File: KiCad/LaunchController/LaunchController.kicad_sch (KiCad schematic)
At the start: 37 parts, among them J1 CONN_ICSP, J13 CONN_7SEG, J2 CONN_USB, J3 USB_B_Micro, U1 FT232RL, U2 ATMEGA2560-16AUR, Y1 HUSG-16.000-20

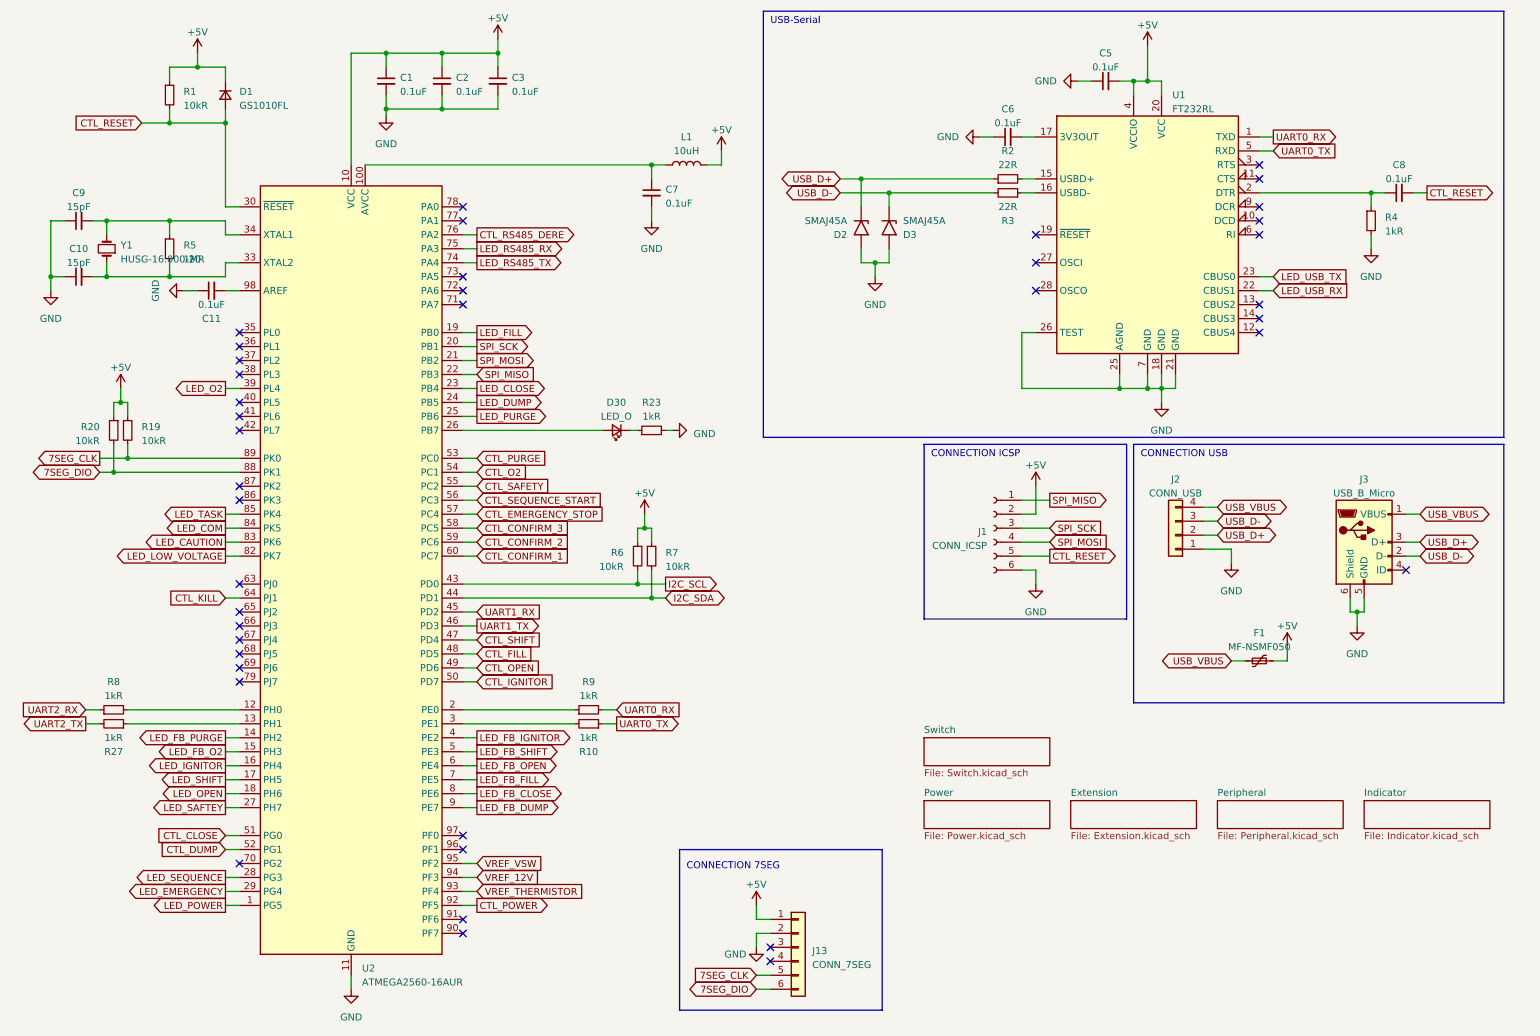
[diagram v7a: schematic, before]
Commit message: USBのTX，RXを統合してACCESSに変更
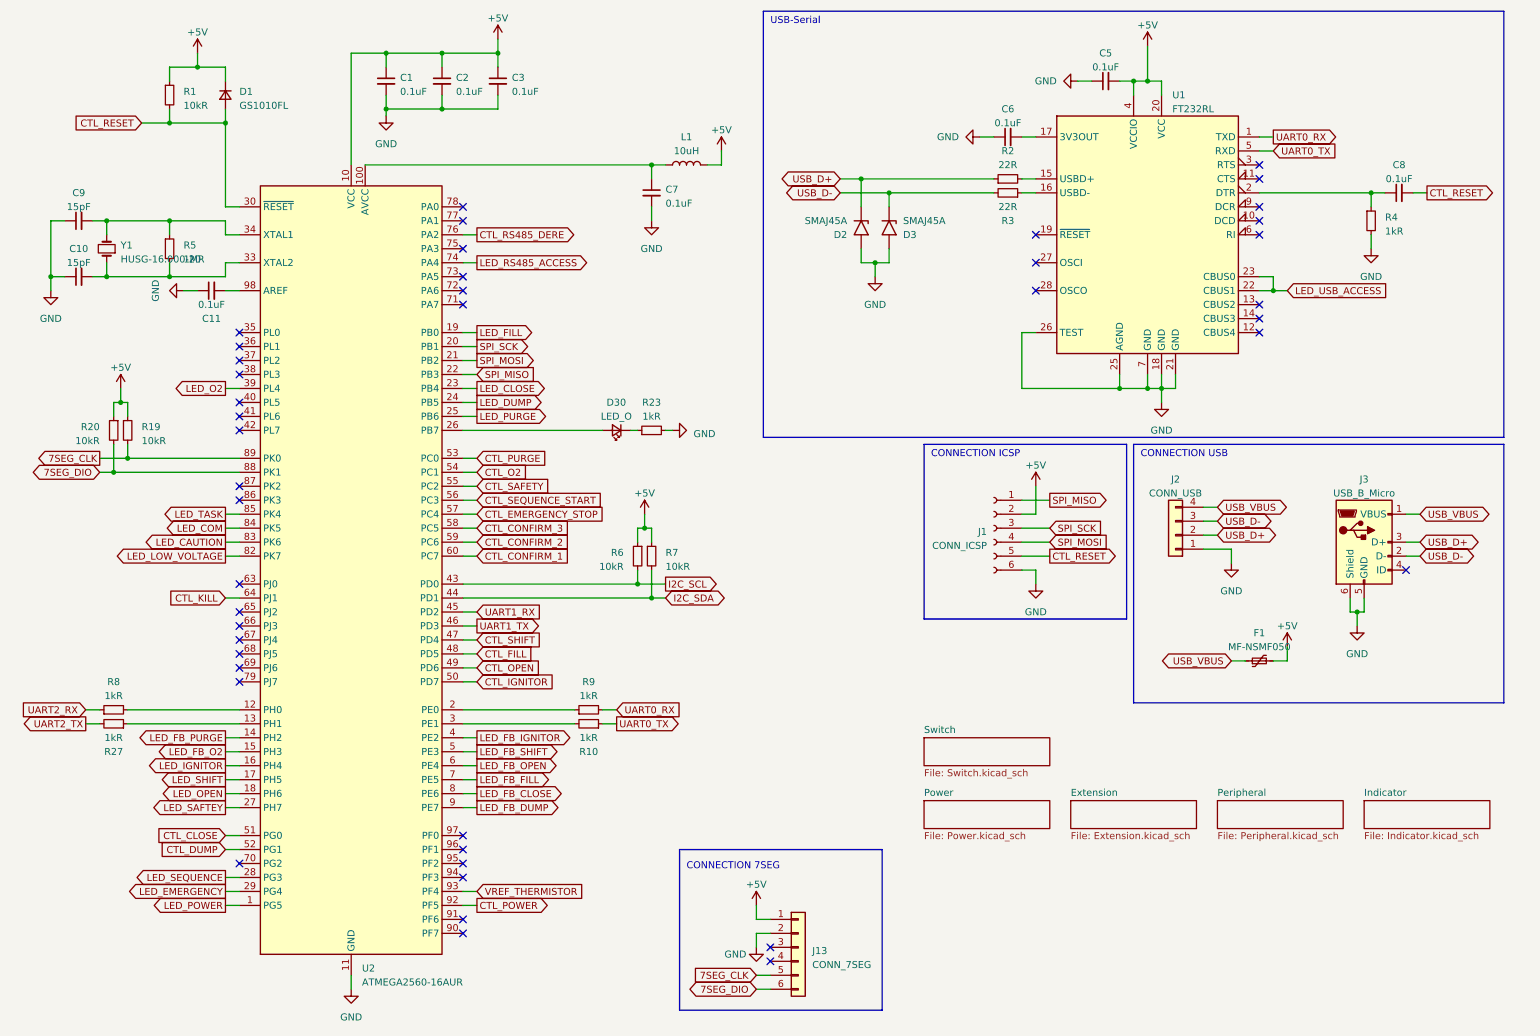
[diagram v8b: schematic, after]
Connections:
- net LED_USB_TX is gone; now on net LED_USB_ACCESS: U1.23 (CBUS0)
- net LED_RS485_RX: no longer names the net of U2.75 (PA3)
- net LED_RS485_TX renamed LED_RS485_ACCESS
- net LED_USB_RX renamed LED_USB_ACCESS
- net VREF_12V: no longer names the net of U2.94 (PF3)
- net VREF_VSW: no longer names the net of U2.95 (PF2)
- no-connect marks 40 -> 43
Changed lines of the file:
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@@
   (junction (at 33.02 83.82) (diameter 0) (color 0 0 0 0)
+  )
+  (junction (at 242.57 63.5) (diameter 0) (color 0 0 0 0)
   )
   (junction (at 41.91 33.02) (diameter 0) (color 0 0 0 0)
@@
   (no_connect (at 95.25 48.26))
   (no_connect (at 54.61 71.12))
+  (no_connect (at 95.25 55.88))
   (no_connect (at 199.39 63.5))
   (no_connect (at 240.03 71.12))
@@
   (no_connect (at 54.61 116.84))
   (no_connect (at 54.61 129.54))
+  (no_connect (at 95.25 170.18))
   (no_connect (at 54.61 99.06))
   (no_connect (at 95.25 180.34))
@@
   (no_connect (at 95.25 60.96))
   (no_connect (at 54.61 83.82))
+  (no_connect (at 95.25 167.64))
   (no_connect (at 95.25 162.56))
   (no_connect (at 240.03 40.64))
@@
     (stroke (width 0) (type default))
   )
-  (wire (pts (xy 95.25 55.88) (xy 97.79 55.88))
-    (stroke (width 0) (type default))
-  )
   (wire (pts (xy 52.07 58.42) (xy 52.07 60.96))
     (stroke (width 0) (type default))
@@
     (stroke (width 0) (type default))
   )
-  (wire (pts (xy 95.25 167.64) (xy 97.79 167.64))
-    (stroke (width 0) (type default))
-  )
   (wire (pts (xy 224.79 81.28) (xy 222.25 81.28))
     (stroke (width 0) (type default))
@@
     (stroke (width 0) (type default))
   )
-  (wire (pts (xy 95.25 170.18) (xy 97.79 170.18))
-    (stroke (width 0) (type default))
-  )
   (wire (pts (xy 41.91 33.02) (xy 52.07 33.02))
     (stroke (width 0) (type default))
@@
     (stroke (width 0) (type default))
   )
+  (wire (pts (xy 242.57 63.5) (xy 245.11 63.5))
+    (stroke (width 0) (type default))
+  )
   (wire (pts (xy 222.25 27.94) (xy 222.25 25.4))
     (stroke (width 0) (type default))
@@
   )
   (wire (pts (xy 95.25 116.84) (xy 127 116.84))
+    (stroke (width 0) (type default))
+  )
+  (wire (pts (xy 242.57 60.96) (xy 242.57 63.5))
     (stroke (width 0) (type default))
   )
@@
     )
   )
-  (global_label "VREF_VSW" (shape input) (at 97.79 167.64 0) (fields_autoplaced)
-    (effects (font (size 1.27 1.27)) (justify left))
-    (property "Intersheetrefs" "${INTERSHEET_REFS}" (at 110.0091 167.64 0)
-      (effects (font (size 1.27 1.27)) (justify left) hide)
-    )
-  )
   (global_label "CTL_PURGE" (shape input) (at 97.79 93.98 0) (fields_autoplaced)
     (effects (font (size 1.27 1.27)) (justify left))
@@
     )
   )
-  (global_label "VREF_12V" (shape input) (at 97.79 170.18 0) (fields_autoplaced)
-    (effects (font (size 1.27 1.27)) (justify left))
-    (property "Intersheetrefs" "${INTERSHEET_REFS}" (at 109.7672 170.18 0)
-      (effects (font (size 1.27 1.27)) (justify left) hide)
-    )
-  )
   (global_label "SPI_MOSI" (shape output) (at 97.79 76.2 0) (fields_autoplaced)
     (effects (font (size 1.27 1.27)) (justify left))
@@
     )
   )
-  (global_label "LED_RS485_TX" (shape output) (at 97.79 58.42 0) (fields_autoplaced)
-    (effects (font (size 1.27 1.27)) (justify left))
-    (property "Intersheetrefs" "${INTERSHEET_REFS}" (at 114.3632 58.42 0)
+  (global_label "LED_RS485_ACCESS" (shape output) (at 97.79 58.42 0) (fields_autoplaced)
+    (effects (font (size 1.27 1.27)) (justify left))
+    (property "Intersheetrefs" "${INTERSHEET_REFS}" (at 119.3827 58.42 0)
       (effects (font (size 1.27 1.27)) (justify left) hide)
     )
@@
     )
   )
-  (global_label "LED_USB_TX" (shape input) (at 242.57 60.96 0) (fields_autoplaced)
-    (effects (font (size 1.27 1.27)) (justify left))
-    (property "Intersheetrefs" "${INTERSHEET_REFS}" (at 256.8452 60.96 0)
-      (effects (font (size 1.27 1.27)) (justify left) hide)
-    )
-  )
   (global_label "USB_D-" (shape bidirectional) (at 232.41 105.41 0) (fields_autoplaced)
     (effects (font (size 1.27 1.27)) (justify left))
@@
     )
   )
-  (global_label "LED_USB_RX" (shape input) (at 242.57 63.5 0) (fields_autoplaced)
-    (effects (font (size 1.27 1.27)) (justify left))
-    (property "Intersheetrefs" "${INTERSHEET_REFS}" (at 257.1476 63.5 0)
+  (global_label "LED_USB_ACCESS" (shape input) (at 245.11 63.5 0) (fields_autoplaced)
+    (effects (font (size 1.27 1.27)) (justify left))
+    (property "Intersheetrefs" "${INTERSHEET_REFS}" (at 264.4047 63.5 0)
       (effects (font (size 1.27 1.27)) (justify left) hide)
     )
@@
       (effects (font (size 1.27 1.27)) (justify left) hide)
     )
-  )
-  (global_label "LED_RS485_RX" (shape output) (at 97.79 55.88 0) (fields_autoplaced)
-    (effects (font (size 1.27 1.27)) (justify left))
-    (property "Intersheetrefs" "${INTERSHEET_REFS}" (at 114.6656 55.88 0)
-      (effects (font (size 1.27 1.27)) (justify left) hide)
-    )
